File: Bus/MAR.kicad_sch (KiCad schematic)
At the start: 2 parts, among them J16 Conn_01x06_Pin, J17 Conn_01x03_Pin

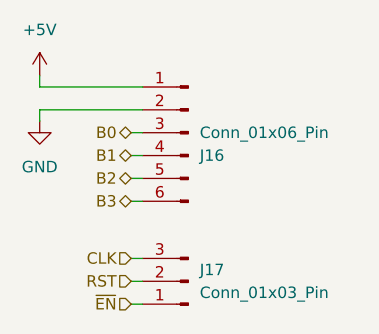
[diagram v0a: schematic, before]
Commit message: Updated bus schmatic pins to match final layouts
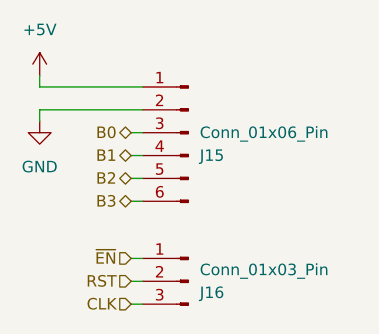
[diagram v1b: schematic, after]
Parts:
- renumbered J16 to J15, J17 to J16
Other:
- moved on the sheet: J16
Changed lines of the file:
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@@
+	(wire
+		(pts
+			(xy 99.06 83.82) (xy 100.33 83.82)
+		)
+		(stroke
+			(width 0)
+			(type default)
+		)
+	)
+	(wire
+		(pts
+			(xy 100.33 62.23) (xy 88.9 62.23)
+		)
+		(stroke
+			(width 0)
+			(type default)
+		)
+	)
+	(wire
+		(pts
+			(xy 100.33 67.31) (xy 99.06 67.31)
+		)
+		(stroke
+			(width 0)
+			(type default)
+		)
+	)
+	(wire
+		(pts
+			(xy 99.06 81.28) (xy 100.33 81.28)
+		)
+		(stroke
+			(width 0)
+			(type default)
+		)
+	)
 	(wire
 		(pts
 			(xy 99.06 78.74) (xy 100.33 78.74)
-		)
-		(stroke
-			(width 0)
-			(type default)
-		)
-	)
-	(wire
-		(pts
-			(xy 100.33 62.23) (xy 88.9 62.23)
-		)
-		(stroke
-			(width 0)
-			(type default)
-		)
-	)
-	(wire
-		(pts
-			(xy 100.33 67.31) (xy 99.06 67.31)
-		)
-		(stroke
-			(width 0)
-			(type default)
-		)
-	)
-	(wire
-		(pts
-			(xy 99.06 81.28) (xy 100.33 81.28)
-		)
-		(stroke
-			(width 0)
-			(type default)
-		)
-	)
-	(wire
-		(pts
-			(xy 99.06 83.82) (xy 100.33 83.82)
 		)
 		(stroke
@@
 	(hierarchical_label "~{EN}"
 		(shape input)
-		(at 99.06 83.82 180)
+		(at 99.06 78.74 180)
 		(fields_autoplaced yes)
 		(effects
@@
 	(hierarchical_label "CLK"
 		(shape input)
-		(at 99.06 78.74 180)
+		(at 99.06 83.82 180)
 		(fields_autoplaced yes)
 		(effects
@@
 		(dnp no)
 		(fields_autoplaced yes)
-		(property "Reference" "#PWR021"
+		(property "Reference" "#PWR018"
 			(at 88.9 69.85 0)
 			(effects
@@
 			(project "bus"
 				(path "/37ae8b13-e183-404e-b70a-681e1af60f55/119f76b4-6f05-4dbd-b43d-328ecfc5c099"
-					(reference "#PWR021")
+					(reference "#PWR018")
 					(unit 1)
 				)
@@
 		(dnp no)
 		(fields_autoplaced yes)
-		(property "Reference" "J16"
+		(property "Reference" "J15"
 			(at 106.68 67.3101 0)
 			(effects
@@
 			(project "bus"
 				(path "/37ae8b13-e183-404e-b70a-681e1af60f55/119f76b4-6f05-4dbd-b43d-328ecfc5c099"
-					(reference "J16")
+					(reference "J15")
 					(unit 1)
 				)
@@
 	(symbol
 		(lib_id "Connector:Conn_01x03_Pin")
-		(at 105.41 81.28 180)
+		(at 105.41 81.28 0)
+		(mirror y)
 		(unit 1)
 		(exclude_from_sim no)
@@
 		(dnp no)
 		(fields_autoplaced yes)
-		(property "Reference" "J17"
-			(at 106.68 80.0099 0)
+		(property "Reference" "J16"
+			(at 106.68 82.5501 0)
 			(effects
 				(font
@@
 		)
 		(property "Value" "Conn_01x03_Pin"
-			(at 106.68 82.5499 0)
+			(at 106.68 80.0101 0)
 			(effects
 				(font
@@
 			(project "bus"
 				(path "/37ae8b13-e183-404e-b70a-681e1af60f55/119f76b4-6f05-4dbd-b43d-328ecfc5c099"
-					(reference "J17")
+					(reference "J16")
 					(unit 1)
 				)
@@
 		(dnp no)
 		(fields_autoplaced yes)
-		(property "Reference" "#PWR020"
+		(property "Reference" "#PWR017"
 			(at 88.9 62.23 0)
 			(effects
@@
 			(project "bus"
 				(path "/37ae8b13-e183-404e-b70a-681e1af60f55/119f76b4-6f05-4dbd-b43d-328ecfc5c099"
-					(reference "#PWR020")
+					(reference "#PWR017")
 					(unit 1)
 				)
